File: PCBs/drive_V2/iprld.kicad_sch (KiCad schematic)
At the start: 74 parts, among them IC1 W25Q16JVUXIQ_TR, IC2 ADS1115IDGSR, J1 SM06B-GHS-TB_LF__SN_, J10 XT60PW-F, J11 12401832E402A, J2 SM06B-GHS-TB_LF__SN_, J3 SM06B-GHS-TB_LF__SN_, J4 SM06B-GHS-TB_LF__SN_, J5 SM06B-GHS-TB_LF__SN_, J6 XT60PW-F, J7 SM06B-GHS-TB_LF__SN_, J8 XT60PW-F, J9 XT30PW-F, U1 AMS1117-3.3, U10 USBLC6-4SC6, U11 4N35, U12 4N35, U13 4N35, U14 4N35, U2 ESP32-S3, U3 4N35, U5 TCA9548APWR, U6 4N35, U7 4N35, U8 4N35, U9 AMS1117-5.0, Y1 7M40000010

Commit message: Add files via upload
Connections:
- net +3.3V: no longer R17.1
- net SCL_LB: now also J2.3; no longer J2.2
- net SCL_LF: now also J1.3; no longer J1.2
- net SCL_RB: now also J4.3; no longer J4.2
- net SCL_RF: now also J3.3; no longer J3.2
- net SDA_LB: now also J2.2; no longer J2.3
- net SDA_LF: now also J1.2; no longer J1.3
- net SDA_RB: now also J4.2; no longer J4.3
- net SDA_RF: now also J3.2; no longer J3.3
- net +FUSE_L: now reaches Fuse_L1.3, Fuse_L1.4, I_LEFT1.1 (IP+), I_LEFT1.2 (IP+)
- net +FUSE_R: now reaches Fuse_R1.3, Fuse_R1.4, I_RIGHT1.1 (IP+), I_RIGHT1.2 (IP+)
- net at C10.2, R2.1, RESET1.1 (NO_1)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: now also R17.1
- no-connect marks 59 -> 60
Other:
- moved on the sheet: LED1, R17
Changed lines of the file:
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@@
 	)
 	(junction
+		(at 516.89 337.82)
+		(diameter 0)
+		(color 0 0 0 0)
+	)
+	(junction
 		(at 114.3 97.79)
 		(diameter 0)
@@
 	)
 	(no_connect
-		(at 353.06 148.59)
-	)
-	(no_connect
 		(at 157.48 111.76)
 	)
@@
 	)
 	(no_connect
+		(at 516.89 350.52)
+	)
+	(no_connect
 		(at 129.54 297.18)
 	)
@@
 	)
 	(no_connect
-		(at 388.62 148.59)
+		(at 567.69 377.19)
 	)
 	(no_connect
@@
 	)
 	(no_connect
+		(at 552.45 350.52)
+	)
+	(no_connect
 		(at 471.17 271.78)
 	)
@@
 	(wire
 		(pts
-			(xy 347.98 146.05) (xy 353.06 146.05)
+			(xy 570.23 336.55) (xy 570.23 347.98)
 		)
 		(stroke
@@
 	(wire
 		(pts
+			(xy 570.23 327.66) (xy 570.23 328.93)
+		)
+		(stroke
+			(width 0)
+			(type default)
+		)
+	)
+	(wire
+		(pts
 			(xy 488.95 248.92) (xy 494.03 248.92)
 		)
@@
 	(wire
 		(pts
+			(xy 556.26 327.66) (xy 570.23 327.66)
+		)
+		(stroke
+			(width 0)
+			(type default)
+		)
+	)
+	(wire
+		(pts
 			(xy 152.4 101.6) (xy 157.48 101.6)
 		)
@@
 	(wire
 		(pts
-			(xy 494.03 337.82) (xy 520.7 337.82)
+			(xy 494.03 337.82) (xy 516.89 337.82)
 		)
 		(stroke
@@
 	(wire
 		(pts
+			(xy 570.23 347.98) (xy 552.45 347.98)
+		)
+		(stroke
+			(width 0)
+			(type default)
+		)
+	)
+	(wire
+		(pts
 			(xy 72.39 278.13) (xy 72.39 276.86)
 		)
@@
 	(wire
 		(pts
+			(xy 516.89 337.82) (xy 516.89 347.98)
+		)
+		(stroke
+			(width 0)
+			(type default)
+		)
+	)
+	(wire
+		(pts
 			(xy 360.68 58.42) (xy 355.6 58.42)
 		)
@@
 	(wire
 		(pts
+			(xy 516.89 337.82) (xy 520.7 337.82)
+		)
+		(stroke
+			(width 0)
+			(type default)
+		)
+	)
+	(wire
+		(pts
 			(xy 360.68 45.72) (xy 360.68 48.26)
 		)
@@
 	(wire
 		(pts
-			(xy 388.62 146.05) (xy 389.89 146.05)
+			(xy 570.23 377.19) (xy 570.23 378.46)
 		)
 		(stroke
@@
 	)
 	(label "SDA_RB"
-		(at 87.63 127 180)
+		(at 87.63 124.46 180)
 		(fields_autoplaced yes)
 		(effects
@@
 	)
 	(label "SDA_LB"
-		(at 43.18 127 180)
+		(at 43.18 124.46 180)
 		(fields_autoplaced yes)
 		(effects
@@
 	)
 	(label "SDA_RF"
-		(at 87.63 97.79 180)
+		(at 87.63 95.25 180)
 		(fields_autoplaced yes)
 		(effects
@@
 		)
 	)
+	(label "+FUSE_L"
+		(at 322.58 71.12 0)
+		(fields_autoplaced yes)
+		(effects
+			(font
+				(size 1.27 1.27)
+			)
+			(justify left bottom)
+		)
+	)
 	(label "SPIWP"
 		(at 516.89 274.32 0)
@@
 	)
 	(label "SCL_RF"
-		(at 87.63 95.25 180)
+		(at 87.63 97.79 180)
 		(fields_autoplaced yes)
 		(effects
@@
 	)
 	(label "SCL_LF"
-		(at 43.18 95.25 180)
+		(at 43.18 97.79 180)
 		(fields_autoplaced yes)
 		(effects
@@
 		)
 	)
+	(label "+FUSE_R"
+		(at 323.85 83.82 0)
+		(fields_autoplaced yes)
+		(effects
+			(font
+				(size 1.27 1.27)
+			)
+			(justify left bottom)
+		)
+	)
 	(label "XTAL_N"
 		(at 471.17 330.2 180)
@@
 	)
 	(label "SCL_RB"
-		(at 87.63 124.46 180)
+		(at 87.63 127 180)
 		(fields_autoplaced yes)
 		(effects
@@
 	)
 	(label "SCL_LB"
-		(at 43.18 124.46 180)
+		(at 43.18 127 180)
 		(fields_autoplaced yes)
 		(effects
@@
 	)
 	(label "SDA_LF"
-		(at 43.18 97.79 180)
+		(at 43.18 95.25 180)
 		(fields_autoplaced yes)
 		(effects
@@
 	(symbol
 		(lib_id "AAA3528ESGCT:AAA3528ESGCT")
-		(at 388.62 146.05 0)
-		(mirror y)
+		(at 516.89 347.98 0)
 		(unit 1)
 		(exclude_from_sim no)
@@
 		(dnp no)
 		(property "Reference" "LED1"
-			(at 370.84 138.43 0)
+			(at 534.67 340.36 0)
 			(effects
 				(font
@@
 		)
 		(property "Value" "AAA3528ESGCT"
-			(at 370.84 140.97 0)
+			(at 534.67 342.9 0)
 			(effects
 				(font
@@
 		)
 		(property "Footprint" "iprl_footprints:AAA3528ESGCT"
-			(at 356.87 240.97 0)
+			(at 548.64 442.9 0)
 			(effects
 				(font
@@
 		)
 		(property "Datasheet" "https://www.arrow.com/en/products/aaa3528esgct/kingbright"
-			(at 356.87 340.97 0)
+			(at 548.64 542.9 0)
 			(effects
 				(font
@@
 		)
 		(property "Description" "Standard LEDs - SMD 3.5mmX2.8mm SMD LED LAMP RED GREEN"
-			(at 388.62 146.05 0)
+			(at 516.89 347.98 0)
 			(effects
 				(font
@@
 		)
 		(property "Height" "2.1"
-			(at 356.87 540.97 0)
+			(at 548.64 742.9 0)
 			(effects
 				(font
@@
 		)
 		(property "Manufacturer_Name" "Kingbright"
-			(at 356.87 640.97 0)
+			(at 548.64 842.9 0)
 			(effects
 				(font
@@
 		)
 		(property "Manufacturer_Part_Number" "AAA3528ESGCT"
-			(at 356.87 740.97 0)
+			(at 548.64 942.9 0)
 			(effects
 				(font
@@
 		)
 		(property "Mouser Part Number" "604-AAA3528ESGCT"
-			(at 356.87 840.97 0)
+			(at 548.64 1042.9 0)
 			(effects
 				(font
@@
 		)
 		(property "Mouser Price/Stock" "https://www.mouser.co.uk/ProductDetail/Kingbright/AAA3528ESGCT?qs=HXFqYaX1Q2ztii0bK20PQg%3D%3D"
-			(at 356.87 940.97 0)
+			(at 548.64 1142.9 0)
 			(effects
 				(font
@@
 		)
 		(property "Arrow Part Number" "AAA3528ESGCT"
-			(at 356.87 1040.97 0)
+			(at 548.64 1242.9 0)
 			(effects
 				(font
@@
 		)
 		(property "Arrow Price/Stock" "https://www.arrow.com/en/products/aaa3528esgct/kingbright?region=nac"
-			(at 356.87 1140.97 0)
+			(at 548.64 1342.9 0)
 			(effects
 				(font
@@
 	(symbol
 		(lib_id "Device:R")
-		(at 344.17 146.05 90)
+		(at 570.23 332.74 0)
 		(unit 1)
 		(exclude_from_sim no)
@@
 		(dnp no)
 		(property "Reference" "R17"
-			(at 344.17 148.59 90)
+			(at 567.69 332.74 90)
 			(effects
 				(font
@@
 		)
 		(property "Value" "56"
-			(at 344.17 143.256 90)
+			(at 573.024 332.74 90)
 			(effects
 				(font
@@
 		)
 		(property "Footprint" "Resistor_SMD:R_0805_2012Metric"
-			(at 344.17 147.828 90)
+			(at 568.452 332.74 90)
 			(effects
 				(font
@@
 		)
 		(property "Datasheet" "~"
-			(at 344.17 146.05 0)
+			(at 570.23 332.74 0)
 			(effects
 				(font
@@
 		)
 		(property "Description" "Resistor"
-			(at 344.17 146.05 0)
+			(at 570.23 332.74 0)
 			(effects
 				(font

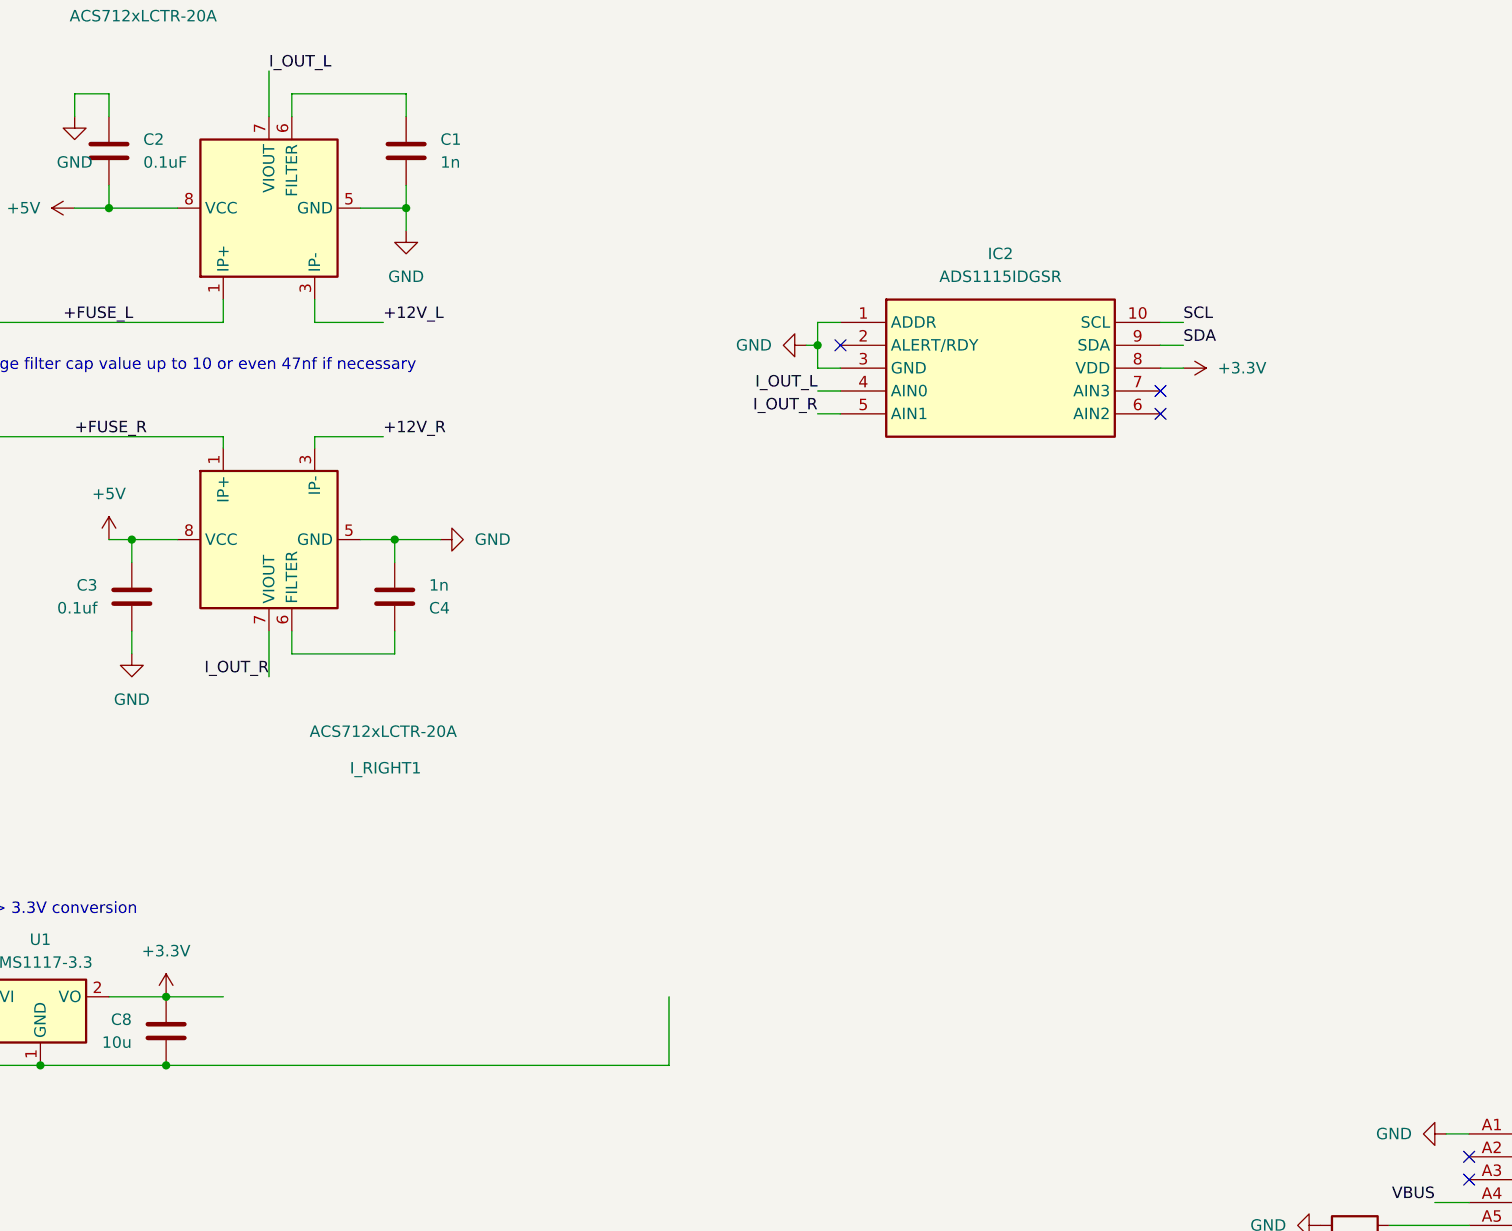
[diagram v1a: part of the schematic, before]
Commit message: changed adc components
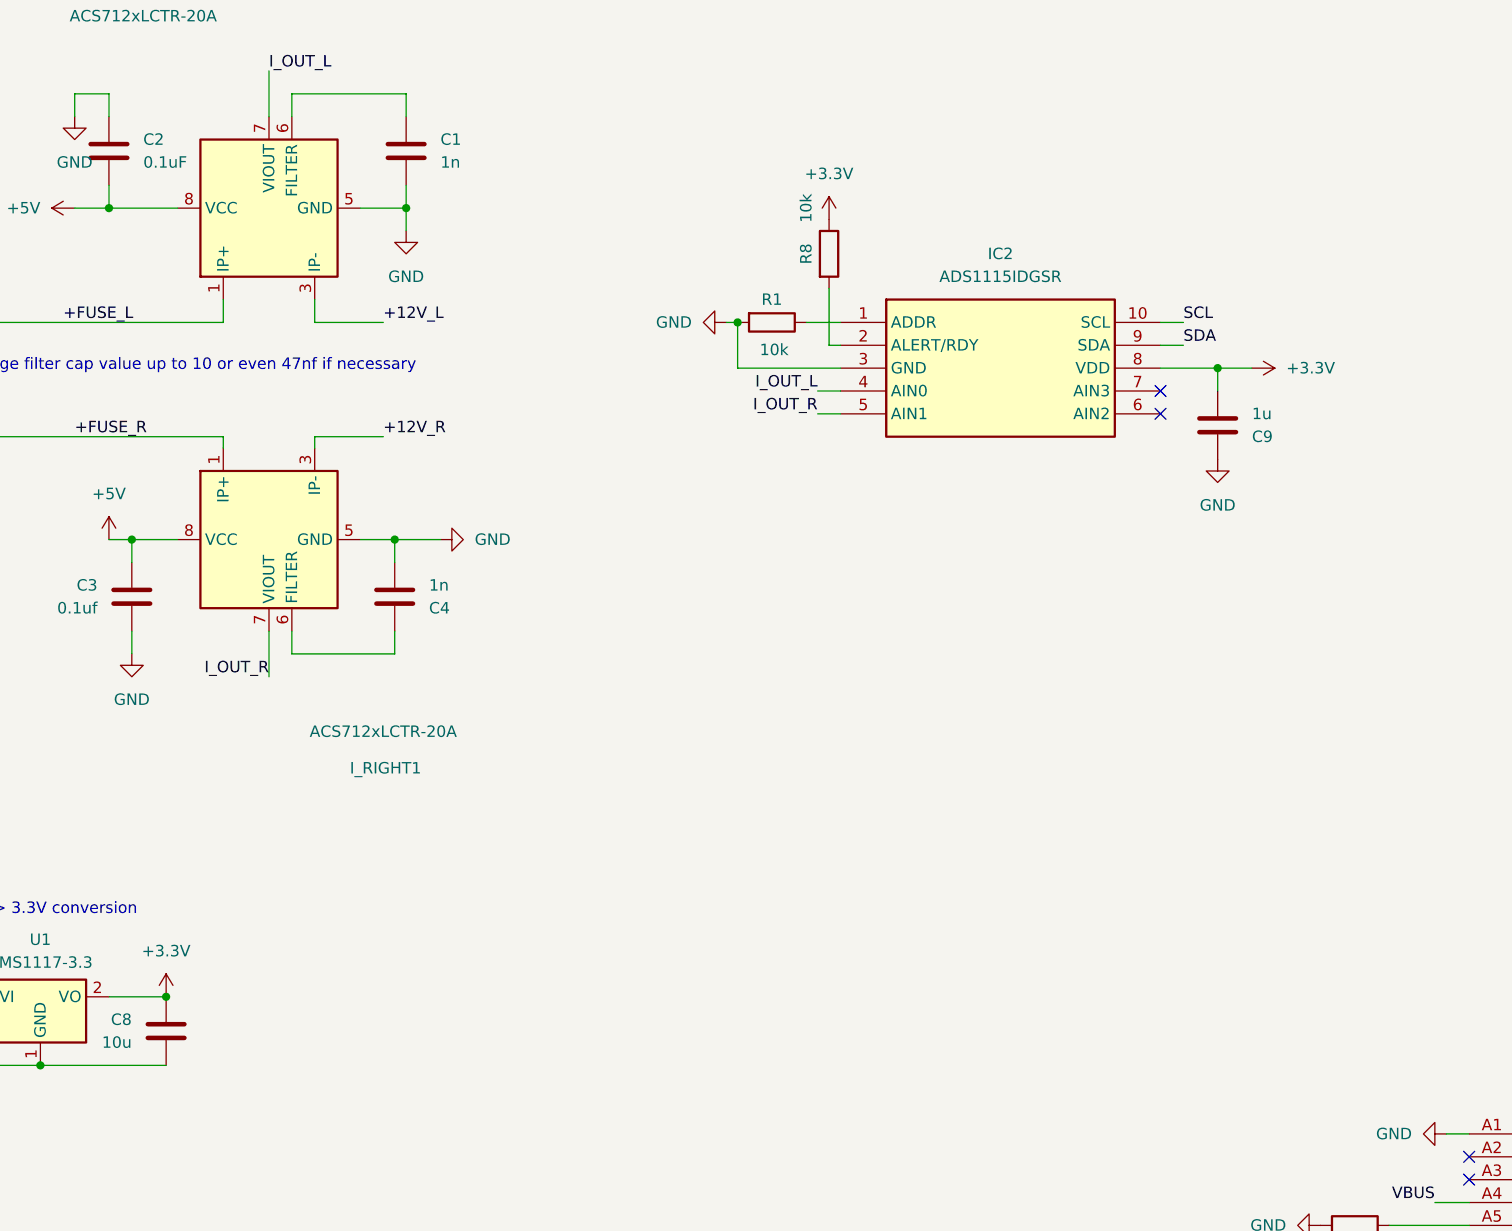
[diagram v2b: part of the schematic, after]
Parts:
- added C9: 1u, Capacitor_SMD:C_0603_1608Metric, symbol Device:C
- added R1, R8: 10k, Resistor_SMD:R_0805_2012Metric, symbol Device:R
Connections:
- net +3.3V: now also C9.1, R8.1
- net GND: now also C9.2, R1.2; no longer IC2.1 (ADDR)
- net at IC2.2 (ALERT/RDY): now also R8.2
- new net: IC2.1 (ADDR), R1.1
- no-connect marks 60 -> 59

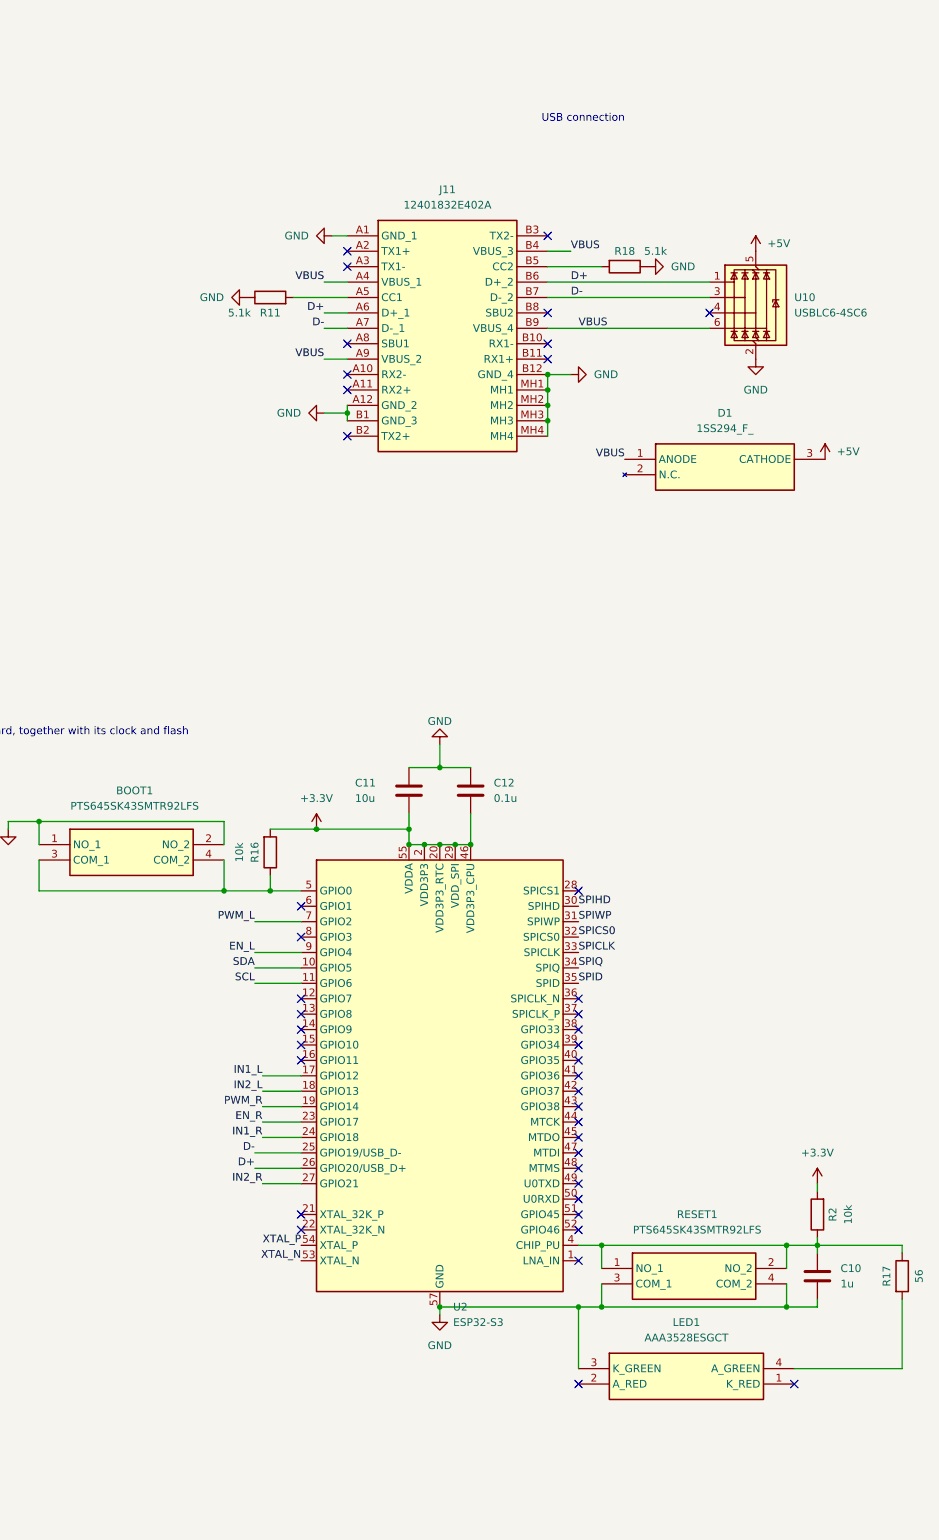
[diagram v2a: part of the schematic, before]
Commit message: New USB C footprint, changed XT inputs to male
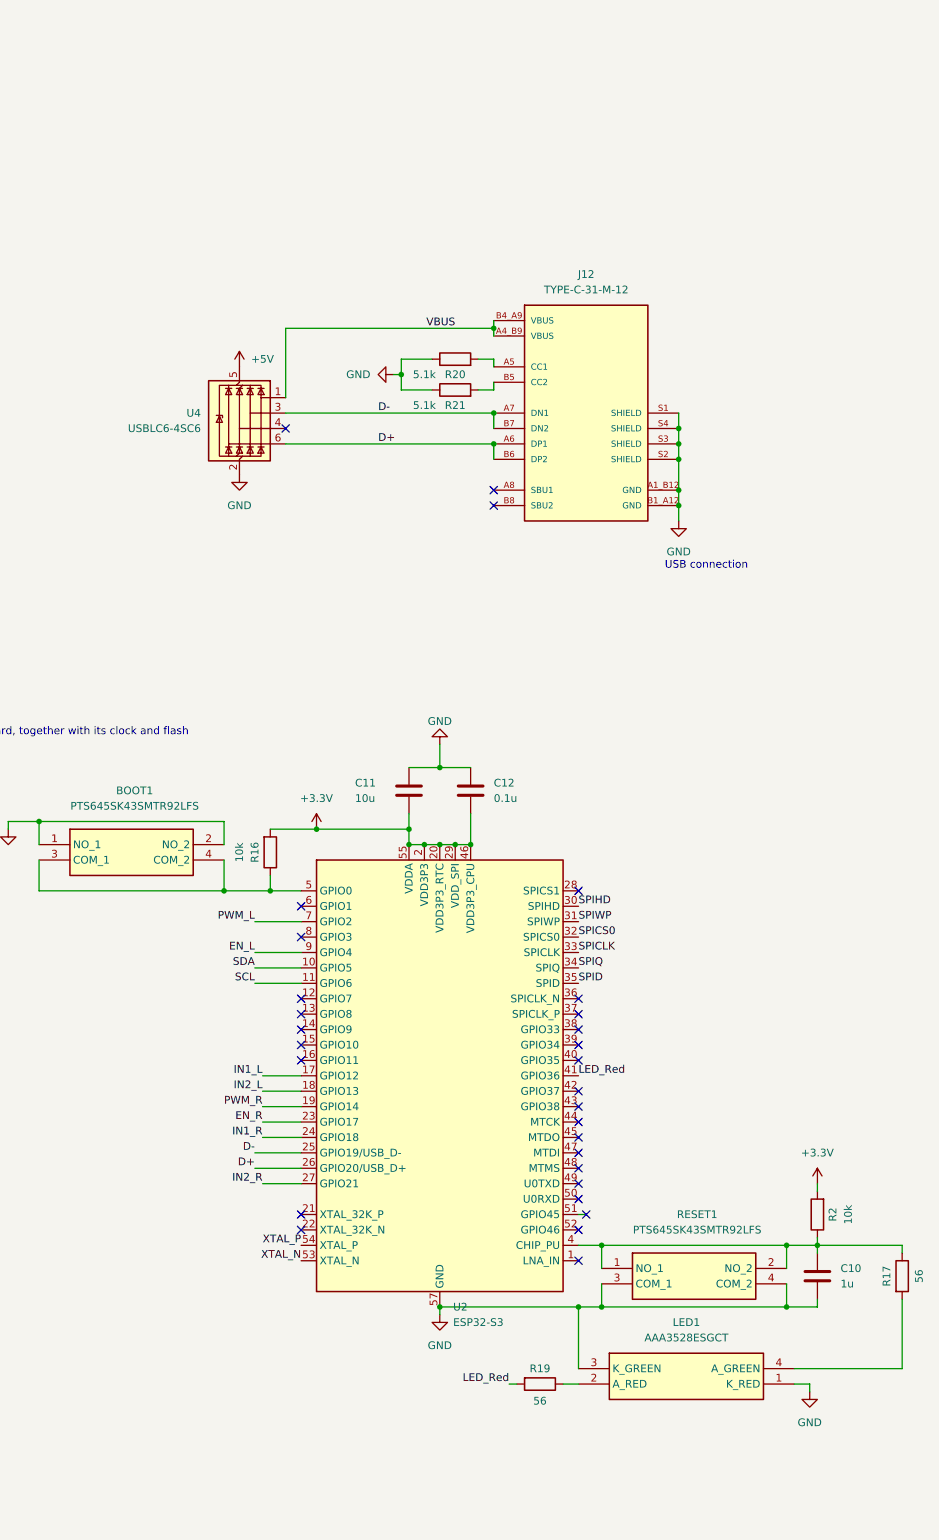
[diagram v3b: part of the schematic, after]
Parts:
- removed D1: 1SS294_F_, iprl_footprints:SOT95P260X140-3N, symbol 1SS294_F_:1SS294_F_
- removed J11: 12401832E402A, iprl_footprints:12401832E402A, symbol 12401832E402A:12401832E402A
- removed R11, R18: 5.1k, Resistor_SMD:R_0805_2012Metric, symbol Device:R
- removed U10: USBLC6-4SC6, Package_TO_SOT_SMD:SOT-23-6, symbol Power_Protection:USBLC6-4SC6
- added J12: TYPE-C-31-M-12, main_lib:TYPE-C-31-M-12, symbol TYPE-C-31-M-12:TYPE-C-31-M-12
- added R19: 56, Resistor_SMD:R_0805_2012Metric, symbol Device:R
- added R20, R21: 5.1k, Resistor_SMD:R_0805_2012Metric, symbol Device:R
- added U4: USBLC6-4SC6, Package_TO_SOT_SMD:SOT-23-6, symbol Power_Protection:USBLC6-4SC6
- J10: footprint iprl_footprints:XT60PWF -> Connector_AMASS:AMASS_XT60PW-M_1x02_P7.20mm_Horizontal
- J9: footprint iprl_footprints:XT30PWF -> Connector_AMASS:AMASS_XT30PW-M_1x02_P2.50mm_Horizontal
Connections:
- net +5V: now also U4.5 (VBUS)
- net D+: now also J12.A6 (DP1), J12.B6 (DP2), U4.6 (I/O4)
- net D-: now also J12.A7 (DN1), J12.B7 (DN2), U4.3 (I/O2)
- net GND: now also LED1.1 (K_RED), J12.A1_B12 (GND), J12.B1_A12 (GND), J12.S1 (SHIELD), J12.S2 (SHIELD), J12.S3 (SHIELD), J12.S4 (SHIELD), R20.1, R21.1, U4.2 (GND)
- net VBUS: now also J12.A4_B9 (VBUS), J12.B4_A9 (VBUS), U4.1 (I/O1)
- net LED_Red: now reaches U2.41 (GPIO36)
- net LED_Red: now also R19.2
- net at LED1.2 (A_RED): now also R19.1
- new net: J12.A5 (CC1), R20.2
- new net: J12.B5 (CC2), R21.2
- no-connect marks 59 -> 48
